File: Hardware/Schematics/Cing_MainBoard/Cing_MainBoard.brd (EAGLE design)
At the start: 100 x 100 mm, 93 parts, among them IC1 L293D, IC2 LM1117T3.3-V, IC3 FT232RL, Q1 16mhz, U2 BMP180, U3 MPU-6050MPU6050

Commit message: MainBoard Upgrade
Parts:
- removed SJ1: (no value), jumper:SJ
- added U$22: OPENSOURCE, Cing Library:OSHW_5MM
- added U$6: BATTERY_CONECTOR_D, Cing Library:BATTERY_CONECTOR_D
- IC2: value LM1117T3.3-V -> LM1117-3.3V
- U$2: value BIG_HEADER -> Header 2
- moved IC2 8.00 mm to (0.92, 47.7)
- moved R31 6.27 mm to (13.5, 17.3)
- moved U$5 3.45 mm to (-44.9, 28.7)
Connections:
- removed net N$28: IRFU9024.S, REVERSE.C, SJ1.2, U$7.+, U$9.COM
- new net N$21: IRFU9024.S, REVERSE.C, U$9.COM
- net GND: now also U$6.-
- net IRFU: now also U$7.+; no longer SJ1.1
- net VCC_MOT: now also U$6.+
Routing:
- net N$28: track 47.2 -> 0.00 mm
- net N$21: track 0.00 -> 36.3 mm
- net GND: track 430.8 -> 456.2 mm
- net VCC_MOT: track 9.63 -> 21.1 mm
- net IRFU: track 72.3 -> 78.4 mm, vias 3 -> 2
- net +3V3: track 555.1 -> 559.6 mm, vias 25 -> 27
- net N$4: track 24.5 -> 28.9 mm
- net SDA: track 46.2 -> 49.4 mm
- net RESET: track 174.7 -> 176.8 mm
- net N$42: track 9.93 -> 10.7 mm
- net BAT+: track 210.1 -> 210.9 mm
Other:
- outline, holes or cut-outs redrawn
- board text added: "Created by RobotCing Team: Veronika Nemjová Stanislav Jochman"
- board text added: "FTDI"
- board text added: "Header 1"
- board text added: "Header 2"
- board text added: "ICSP"
- board text added: "Motor Switch"
- board text added: "Robot Switch"

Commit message: upgrading board
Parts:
- removed C6: 100uf, rcl:E3,5-8
- added JP2: ServoA, pinhead:1X03
- added JP3: ServoB, pinhead:1X03
- added JP4: ServoC, pinhead:1X03
- added R21, R23: PHOTOCELL1, LDR:LDR_OFFBOARD
- added R29, R32: 1k, rcl:R1206
- moved C4 19.5 mm to (-3.00, 35.5), turned to 270 degrees
- moved C5 7.62 mm to (25.9, 36.2)
- moved R26 7.62 mm to (29.3, 44.9)
- moved U$22 2.57 mm to (29.6, 42.9)
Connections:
- removed net HD_A7: U$1.A7, U$2.A7
- new net A7: R21.2, R32.1, U$1.A7, U$2.A7
- net +3V3: now also R29.2, R32.2; no longer C6.+
- net A6: now also R23.2, R29.1
- net D6: now also JP4.1
- net GND: now also JP2.3, JP3.3, JP4.3, R21.1, R23.1; no longer C6.-
- net IN_A1: now also JP3.1
- net IN_A2: now also JP2.1
- net VCC_MOT: now also JP2.2, JP3.2, JP4.2
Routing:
- net A6: track 36.7 -> 157.1 mm, vias 0 -> 6
- net A7: track 0.00 -> 110.7 mm, vias 0 -> 7
- net VCC_MOT: track 21.1 -> 117.4 mm, vias 0 -> 3
- net IN_A1: track 53.1 -> 121.9 mm, vias 2 -> 8
- net IN_A2: track 56.8 -> 115.0 mm, vias 1 -> 3
- net GND: track 456.2 -> 512.5 mm
- net +3V3: track 559.6 -> 597.8 mm
- net HD_A7: track 36.3 -> 0.00 mm, vias 2 -> 0
- net N$42: track 10.7 -> 20.3 mm
- net SCK: track 137.3 -> 146.5 mm
- net D6: track 99.7 -> 103.8 mm
- net N$2: track 82.8 -> 80.0 mm
- net VUSB: track 34.1 -> 35.7 mm
- net D-: track 26.3 -> 25.6 mm
- net N$39: track 39.8 -> 39.2 mm
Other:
- board text added: "Created by RobotCing Team: Veronika Nemjová Stanislav Jochman Designed in Slovakia"
- board text removed: "Created by RobotCing Team: Veronika Nemjová Stanislav Jochman"

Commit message: Final
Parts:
- added POT: 100k, pot:RJ9W
- added TSOP4838: TSOP4838, Cing Library:TSOP18XX
- moved LS1 2.00 mm to (25.0, 12.0)
- moved LS2 2.00 mm to (25.0, -12.0)
- moved U$13 1.00 mm to (25.0, 18.6)
- moved U$14 1.00 mm to (25.0, -18.6)
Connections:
- net +3V3: now also POT.E, TSOP4838.VCC
- net A1: now also POT.S
- net D4: now also TSOP4838.OUT
- net GND: now also POT.A, TSOP4838.GND
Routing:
- net A1: track 18.1 -> 80.2 mm, vias 0 -> 2
- net D4: track 64.4 -> 114.7 mm, vias 2 -> 8
- net +3V3: track 597.8 -> 642.0 mm, vias 27 -> 29
- net N$45: track 26.2 -> 21.6 mm
- net A7: track 110.7 -> 108.2 mm
- net N$24: track 21.5 -> 23.7 mm
- net N$22: track 3.56 -> 5.51 mm
- net N$10: track 39.7 -> 41.6 mm
- net GND: track 512.5 -> 513.1 mm

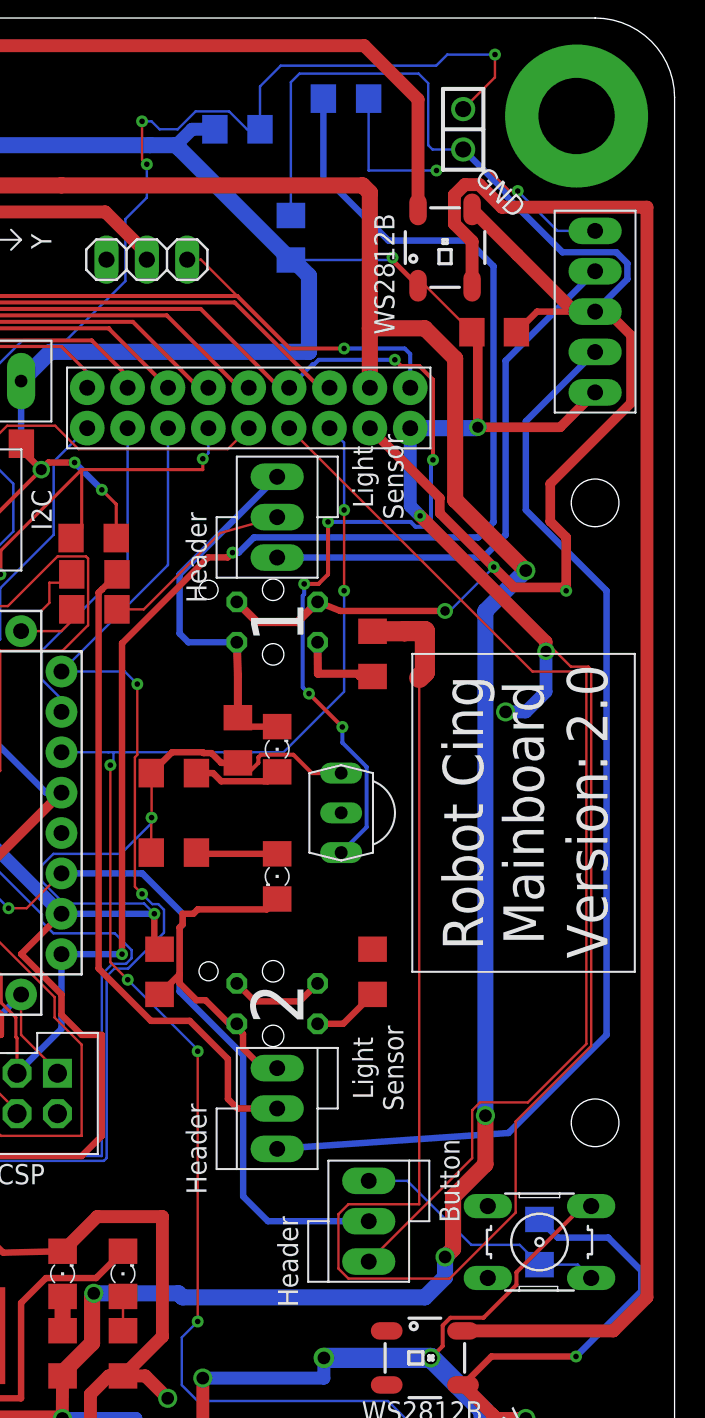
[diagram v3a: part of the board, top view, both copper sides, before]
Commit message: board change
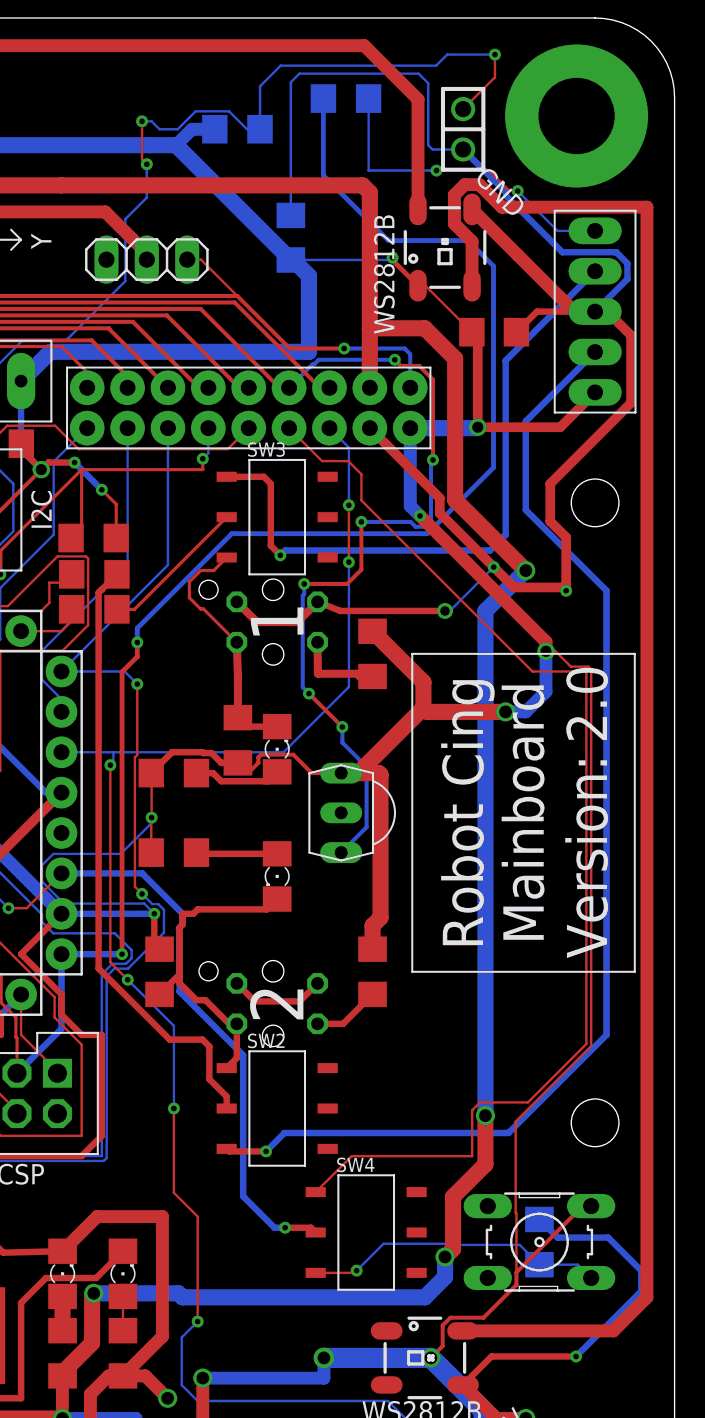
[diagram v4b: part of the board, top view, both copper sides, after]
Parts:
- removed U$13, U$14: CONNECTOR_LIGHT_SENSOR, Cing Library:CONNECTOR_LIGHT_SENSOR
- removed U$15: CONNECTOR_BUTTON, Cing Library:CONNECTOR_BUTTON
- added SW2, SW3, SW4: (no value), Cing Library:USB_SWITCH
- R1, R12, R13, R14, R15, R30, R31: value 10k -> 1k
- R22, R6: value 1k -> 100
- R24, R25: value 330 -> 100
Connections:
- net A6: now also SW4.COM1; no longer U$15.COM
- net BUTTON: now also SW4.CH1B; no longer U$15.BUTTON
- net HD_A6: now also SW4.CH1A; no longer U$15.HEADER
- net N$10: now also SW2.COM1; no longer U$14.COM
- net N$24: now also SW3.CH1B; no longer U$13.LIGHTSENSOR
- net N$31: now also SW3.CH1A; no longer U$13.HEADER
- net N$40: now also SW2.CH1B; no longer U$14.HEADER
- net N$43: now also SW3.COM1; no longer U$13.COM
- net N$45: now also SW2.CH1A; no longer U$14.LIGHTSENSOR
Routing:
- net +3V3: track 642.0 -> 617.2 mm
- net N$24: track 23.7 -> 15.6 mm
- net N$31: track 33.9 -> 41.3 mm, vias 0 -> 1
- net N$40: track 70.2 -> 73.9 mm, vias 0 -> 1
- net A6: track 157.1 -> 154.1 mm, vias 6 -> 7
- net N$10: track 41.6 -> 38.6 mm
- net N$43: track 12.2 -> 9.31 mm
- net BUTTON: track 16.5 -> 19.0 mm, vias 0 -> 1
- net HD_A6: track 69.6 -> 72.0 mm
- net SCK: track 146.5 -> 144.1 mm
- net N$45: track 21.6 -> 20.3 mm
